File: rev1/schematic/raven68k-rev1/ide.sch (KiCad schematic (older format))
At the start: 10 parts

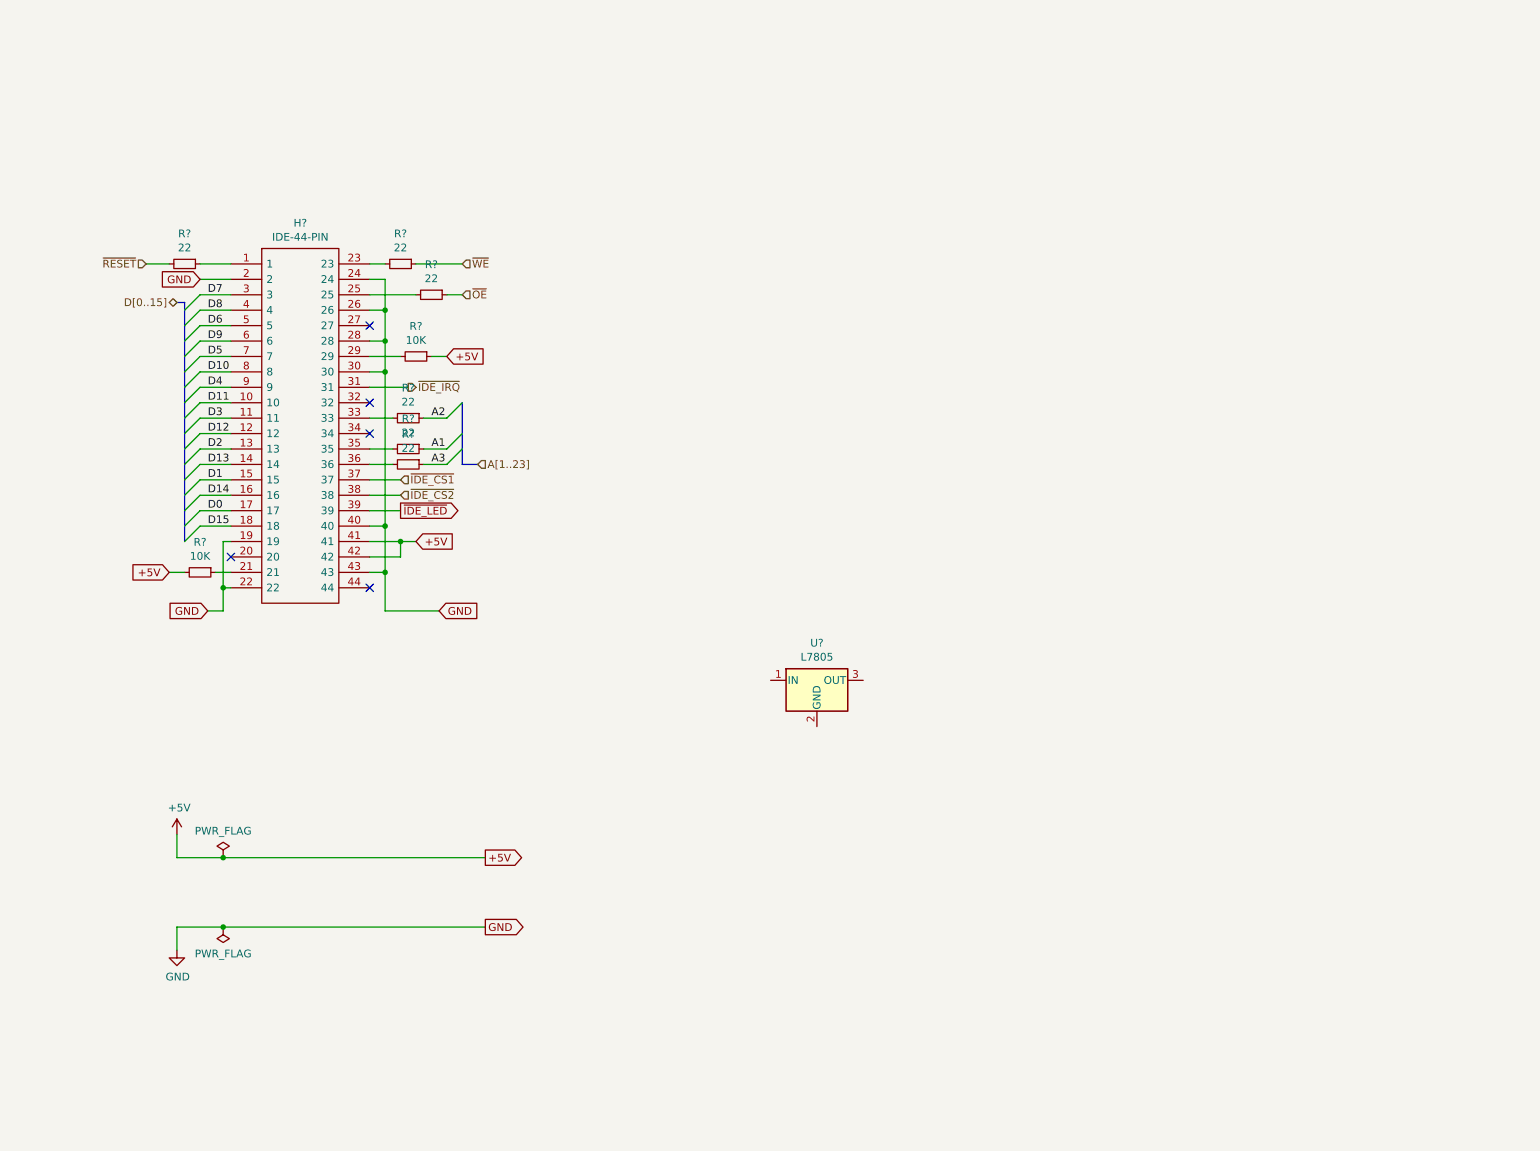
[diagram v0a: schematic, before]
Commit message: added buffers
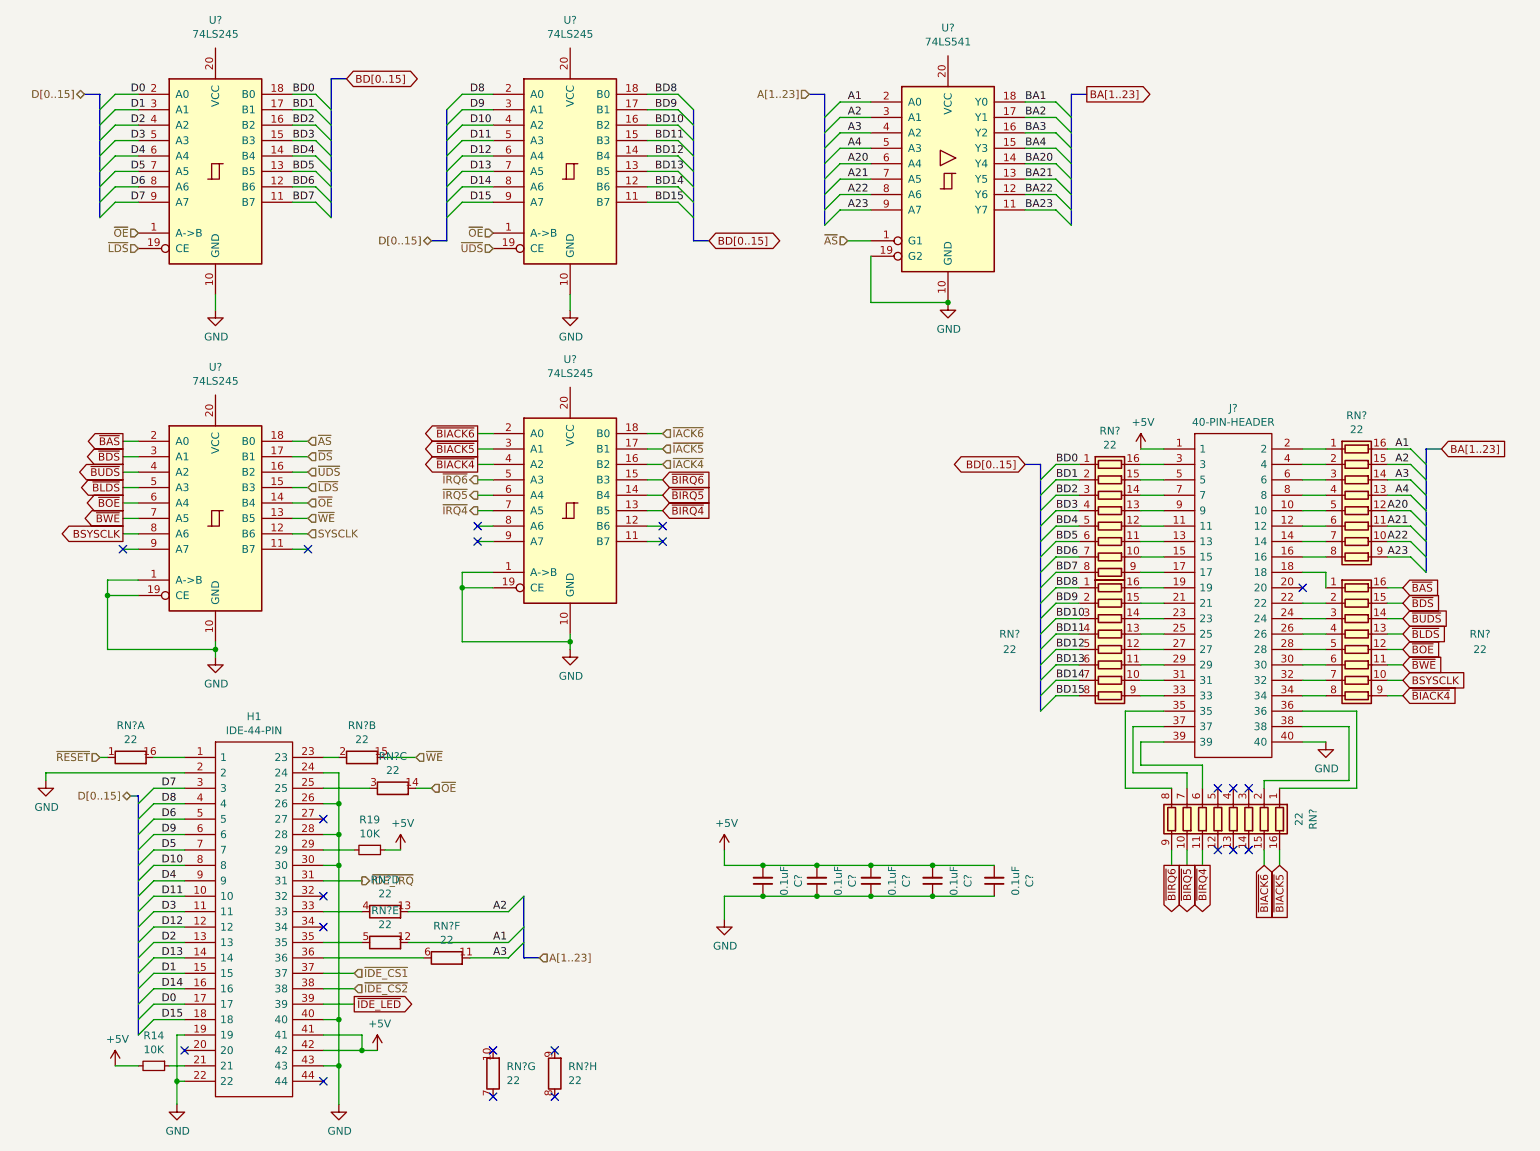
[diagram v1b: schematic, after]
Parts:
- removed R? (x6): 22, symbol Device:R_Small
- removed U?: L7805, symbol Regulator_Linear:L7805
- added C? (x5): 0.1uF, symbol Device:C_Small
- added J?: 40-PIN-HEADER, SHDR40W66P254_2X20_5829X914X986P, symbol custom:40-PIN-HEADER
- added RN? (x5): 22, symbol Device:R_Pack08
- added RN? (x8): 22, symbol Device:R_Pack08_Split
- added U? (x4): 74LS245, symbol 74xx:74LS245
- added U?: 74LS541, symbol 74xx:74LS541
- gave numbers to parts that had none: 3
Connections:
- net +5V: now also C?.2, C?.2, C?.2, C?.2, C?.2, J?.1
- net A1: now also RN?.12 (R5.2), RN?.16 (R1.2), U?.2 (A0)
- net A2: now also RN?.13 (R4.2), RN?.15 (R2.2), U?.3 (A1)
- net A3: now also RN?.11 (R6.2), RN?.14 (R3.2), U?.4 (A2)
- net D0: now also U?.2 (A0)
- net D1: now also U?.3 (A1)
- net D10: now also U?.4 (A2)
- net D11: now also U?.5 (A3)
- net D12: now also U?.6 (A4)
- net D13: now also U?.7 (A5)
- net D14: now also U?.8 (A6)
- net D15: now also U?.9 (A7)
- net D2: now also U?.4 (A2)
- net D3: now also U?.5 (A3)
- net D4: now also U?.6 (A4)
- net D5: now also U?.7 (A5)
- net D6: now also U?.8 (A6)
- net D7: now also U?.9 (A7)
- net D8: now also U?.2 (A0)
- net D9: now also U?.3 (A1)
- net GND: now also C?.1, C?.1, C?.1, C?.1, C?.1, J?.40, U?.1 (A->B), U?.1 (A->B), U?.10 (GND), U?.10 (GND), U?.10 (GND), U?.10 (GND), U?.10 (GND), U?.19 (CE), U?.19 (CE), U?.19 (G2)
- net ~OE: now also RN?.14 (R3.2), U?.1 (A->B), U?.1 (A->B), U?.14 (B4)
- net ~RESET: now also RN?.1 (R1.1)
- net ~WE: now also RN?.15 (R2.2), U?.13 (B5)
- net at H1.1: now also RN?.16 (R1.2)
- net at H1.23: now also RN?.2 (R2.1)
- net at H1.25: now also RN?.3 (R3.1)
- net at H1.33: now also RN?.4 (R4.1)
- net at H1.35: now also RN?.5 (R5.1)
- net at H1.36: now also RN?.6 (R6.1)
- new net: J?.10, RN?.5 (R5.1)
- new net: J?.11, RN?.12 (R5.2)
- new net: J?.12, RN?.6 (R6.1)
- new net: J?.13, RN?.11 (R6.2)
- new net: J?.14, RN?.7 (R7.1)
- new net: J?.15, RN?.10 (R7.2)
- new net: J?.16, RN?.8 (R8.1)
- new net: J?.17, RN?.9 (R8.2)
- new net: J?.18, RN?.1 (R1.1)
- new net: J?.19, RN?.16 (R1.2)
- new net: J?.2, RN?.1 (R1.1)
- new net: J?.21, RN?.15 (R2.2)
- new net: J?.22, RN?.2 (R2.1)
- new net: J?.23, RN?.14 (R3.2)
- new net: J?.24, RN?.3 (R3.1)
- new net: J?.25, RN?.13 (R4.2)
- new net: J?.26, RN?.4 (R4.1)
- new net: J?.27, RN?.12 (R5.2)
- new net: J?.28, RN?.5 (R5.1)
- new net: J?.29, RN?.11 (R6.2)
- new net: J?.3, RN?.16 (R1.2)
- new net: J?.30, RN?.6 (R6.1)
- new net: J?.31, RN?.10 (R7.2)
- new net: J?.32, RN?.7 (R7.1)
- new net: J?.33, RN?.9 (R8.2)
- new net: J?.34, RN?.8 (R8.1)
- new net: J?.35, RN?.8 (R8.1)
- new net: J?.36, RN?.1 (R1.1)
- new net: J?.37, RN?.7 (R7.1)
- new net: J?.38, RN?.2 (R2.1)
- new net: J?.39, RN?.6 (R6.1)
- new net: J?.4, RN?.2 (R2.1)
- new net: J?.5, RN?.15 (R2.2)
- new net: J?.6, RN?.3 (R3.1)
- new net: J?.7, RN?.14 (R3.2)
- new net: J?.8, RN?.4 (R4.1)
- new net: J?.9, RN?.13 (R4.2)
- new net A20: RN?.12 (R5.2), U?.6 (A4)
- new net A21: RN?.11 (R6.2), U?.7 (A5)
- new net A22: RN?.10 (R7.2), U?.8 (A6)
- new net A23: RN?.9 (R8.2), U?.9 (A7)
- new net A4: RN?.13 (R4.2), U?.5 (A3)
- new net BA1: U?.18 (Y0)
- new net BA2: U?.17 (Y1)
- new net BA20: U?.14 (Y4)
- new net BA21: U?.13 (Y5)
- new net BA22: U?.12 (Y6)
- new net BA23: U?.11 (Y7)
- new net BA3: U?.16 (Y2)
- new net BA4: U?.15 (Y3)
- new net BD0: RN?.1 (R1.1), U?.18 (B0)
- new net BD1: RN?.2 (R2.1), U?.17 (B1)
- new net BD10: RN?.3 (R3.1), U?.16 (B2)
- new net BD11: RN?.4 (R4.1), U?.15 (B3)
- new net BD12: RN?.5 (R5.1), U?.14 (B4)
- new net BD13: RN?.6 (R6.1), U?.13 (B5)
- new net BD14: RN?.7 (R7.1), U?.12 (B6)
- new net BD15: RN?.8 (R8.1), U?.11 (B7)
- new net BD2: RN?.3 (R3.1), U?.16 (B2)
- new net BD3: RN?.4 (R4.1), U?.15 (B3)
- new net BD4: RN?.5 (R5.1), U?.14 (B4)
- new net BD5: RN?.6 (R6.1), U?.13 (B5)
- new net BD6: RN?.7 (R7.1), U?.12 (B6)
- new net BD7: RN?.8 (R8.1), U?.11 (B7)
- new net BD8: RN?.1 (R1.1), U?.18 (B0)
- new net BD9: RN?.2 (R2.1), U?.17 (B1)
- new net BSYSCLK: RN?.10 (R7.2), U?.8 (A6)
- new net SYSCLK: U?.12 (B6)
- new net ~AS: U?.1 (G1), U?.18 (B0)
- new net ~BAS: RN?.16 (R1.2), U?.2 (A0)
- new net ~BDS: RN?.15 (R2.2), U?.3 (A1)
- new net ~BIACK4: RN?.9 (R8.2), U?.4 (A2)
- new net ~BIACK5: RN?.16 (R1.2), U?.3 (A1)
- new net ~BIACK6: RN?.15 (R2.2), U?.2 (A0)
- new net ~BIRQ4: RN?.11 (R6.2), U?.13 (B5)
- new net ~BIRQ5: RN?.10 (R7.2), U?.14 (B4)
- new net ~BIRQ6: RN?.9 (R8.2), U?.15 (B3)
- new net ~BLDS: RN?.13 (R4.2), U?.5 (A3)
- new net ~BOE: RN?.12 (R5.2), U?.6 (A4)
- new net ~BUDS: RN?.14 (R3.2), U?.4 (A2)
- new net ~BWE: RN?.11 (R6.2), U?.7 (A5)
- new net ~DS: U?.17 (B1)
- new net ~IACK4: U?.16 (B2)
- new net ~IACK5: U?.17 (B1)
- new net ~IACK6: U?.18 (B0)
- new net ~IRQ4: U?.7 (A5)
- new net ~IRQ5: U?.6 (A4)
- new net ~IRQ6: U?.5 (A3)
- new net ~LDS: U?.15 (B3), U?.19 (CE)
- new net ~UDS: U?.16 (B2), U?.19 (CE)
- no-connect marks 5 -> 22
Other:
- moved on the sheet: H1, R14, R19

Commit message: upgrade to KiCad 6, first shot at layout
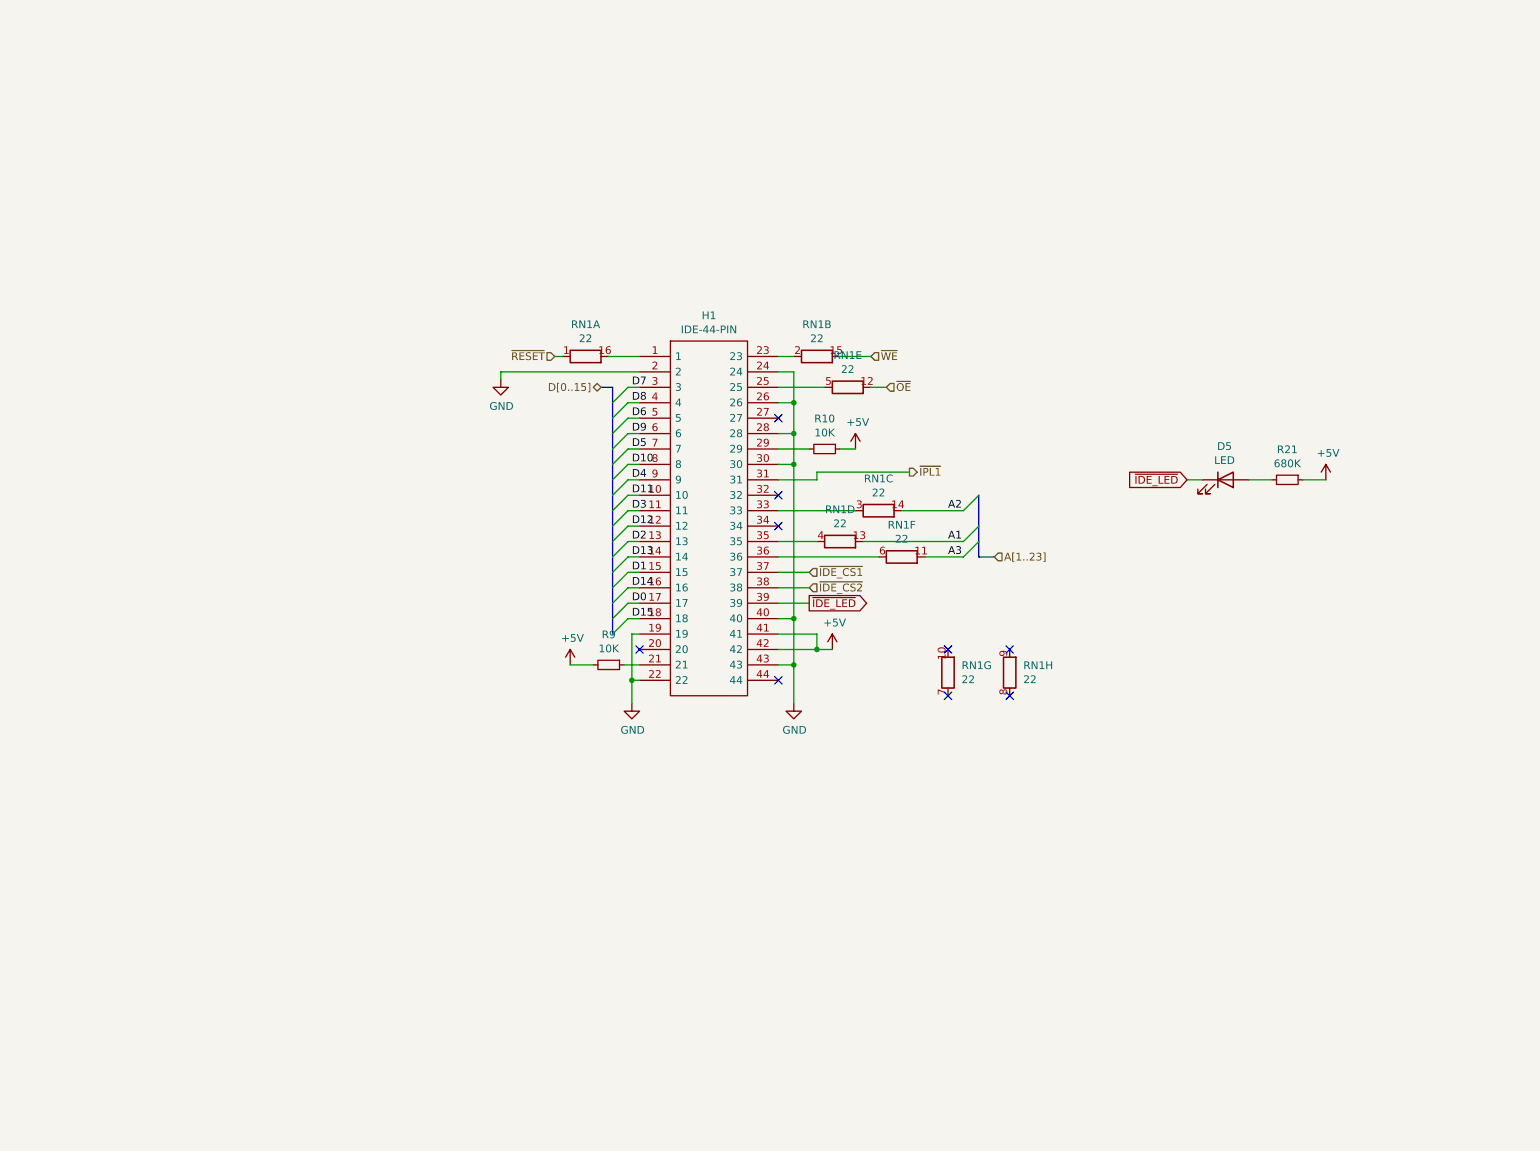
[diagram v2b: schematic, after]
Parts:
- removed C? (x5): 0.1uF, symbol Device:C_Small
- removed J?: 40-PIN-HEADER, SHDR40W66P254_2X20_5829X914X986P, symbol custom:40-PIN-HEADER
- removed RN? (x5): 22, symbol Device:R_Pack08
- removed U? (x4): 74LS245, symbol 74xx:74LS245
- removed U?: 74LS541, symbol 74xx:74LS541
- added D5: LED, symbol Device:LED
- added R21: 680K, symbol Device:R_Small
- H1: footprint HDRV44W80P200_2X22_4400X400X550P -> raven68k-rev1:SHDR40W66P254_2X20_5829X914X986P
- RN1: renamed from RN?; footprint (none) -> Package_DIP:DIP-16_W7.62mm_Socket_LongPads
- renumbered R19 to R10, R14 to R9
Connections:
- net +5V: now also R21.1
- net A1: now also RN1.13 (R4.2); no longer RN1.12 (R5.2)
- net A2: now also RN1.14 (R3.2); no longer RN1.13 (R4.2)
- net ~IDE_LED: now also D5.1 (K)
- net ~OE: now also RN1.12 (R5.2); no longer RN1.14 (R3.2)
- net at H1.25: now also RN1.5 (R5.1); no longer RN1.3 (R3.1)
- net at H1.33: now also RN1.3 (R3.1); no longer RN1.4 (R4.1)
- net at H1.35: now also RN1.4 (R4.1); no longer RN1.5 (R5.1)
- net ~IDE_IRQ renamed ~IPL1
- new net: D5.2 (A), R21.2
- no-connect marks 22 -> 9
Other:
- moved on the sheet: H1, R10, R9, RN1A, RN1B, RN1F, RN1G, RN1H
